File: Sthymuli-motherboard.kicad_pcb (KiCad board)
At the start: 2 copper layers, 176.5 x 154.2 mm, 270 parts, among them J1 USB_C_Receptacle_USB2.0_16P, J2 Conn_01x09, J3 Conn_01x03, J4 Conn_01x06, Q1 Q_NMOS_Depletion_GSD, Q10 NX7002AK, Q11 NX7002AK, Q12 NX7002AK, Q13 NX7002AK, Q14 NX7002AK, Q15 NX7002AK, Q2 Q_NMOS_Depletion_GSD, Q3 Q_NMOS_Depletion_GSD, Q4 Q_NMOS_Depletion_GSD, Q5 Q_NMOS_Depletion_GSD, Q6 Q_NMOS_Depletion_GSD, Q7 PMOS, Q8 NX7002AK, Q9 NX7002AK, SW1 SW_Push, SW10 SW_Push, SW2 SW_Push, SW3 SW_Push, SW4 SW_Push, SW5 SW_Push, SW6 SW_Push, SW7 SW_Push, SW8 SW_Push, SW9 SW_Push, U1 ESP32-S3-WROOM-1, U10 74HC4051, U11 MCP6L01x-xOT, U12 74HC4051, U13 LSM6DS3, U14 LSM6DS3, U15 ITR9909, U16 ITR9909, U17 ITR9909, U18 ITR9909, U19 ITR9909, U2 AP2112K-3.3, U20 ITR9909, U21 ITR9909, U22 ITR9909, U3 BQ76905RGRR, U4 AP62300WU, U5 BQ25713, U6 AP62300WU, U7 MCP23017_SO, U8 AP22913CN4, U9 IRM-H6xxT

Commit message: starting from scratch the routing. autorouter was not good
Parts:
- removed BT1, BT2, BT3: Battery_Cell, sthymuli:Battery_Holder_18650_robop
- removed C10, C11, C12, C13, C14, C15, C16, C17, C18, C19, C20, C21, C22, C23, C24, C25, C77, C8, C9: 100nF, Capacitor_SMD:C_0402_1005Metric
- removed D10, D11, D12, D13, D14, D15, D16, D17, D18, D19, D20, D21, D22, D23, D24, D25, D8, D9: WS2812B, LED_SMD:LED_WS2812B_PLCC4_5.0x5.0mm_P3.2mm
- removed D26, D27, D28: D_Schottky, Diode_SMD:D_SOD-123F
- removed F1, F2, F3: Fuse, Resistor_SMD:R_0805_2012Metric
- removed Q10, Q11, Q12, Q13, Q14, Q15: NX7002AK, Package_TO_SOT_SMD:SOT-23
- removed R52, R53, R54, R55, R56, R57: 3K3, Capacitor_SMD:C_0201_0603Metric
- removed R62, R63, R64, R65, R66, R67: 27R, Capacitor_SMD:C_0201_0603Metric
- removed SW10, SW5, SW6, SW7, SW8, SW9: SW_Push, sthymuli:XKB5858
- removed U13: LSM6DS3, Package_LGA:LGA-14_3x2.5mm_P0.5mm_LayoutBorder3x4y
- removed the U16 at (81.2, 89.6)
- removed U17, U18: ITR9909, sthymuli:ITR_9909_Horizontal
- removed U20, U21, U22: ITR9909, sthymuli:ITR_9909_Vertical
- added J11: Conn_02x08_Counter_Clockwise, Connector_PinSocket_2.54mm:PinSocket_2x08_P2.54mm_Vertical_SMD, B.Cu at (134.6, 75.5)
- added J12: Conn_02x08_Counter_Clockwise, Connector_PinSocket_2.54mm:PinSocket_2x08_P2.54mm_Vertical_SMD, B.Cu at (175.2, 75.5)
- added J8: Conn_02x08_Counter_Clockwise, Connector_PinSocket_2.54mm:PinSocket_2x08_P2.54mm_Vertical_SMD, B.Cu at (208.8, 103.4)
- J2: footprint Connector_PinHeader_2.54mm:PinHeader_1x09_P2.54mm_Vertical -> Connector_PinSocket_2.54mm:PinSocket_1x09_P2.54mm_Vertical_SMD_Pin1Left; moved to B.Cu
- J3: footprint Connector_PinHeader_2.54mm:PinHeader_1x03_P2.54mm_Vertical -> Connector_PinSocket_2.54mm:PinSocket_1x03_P2.54mm_Vertical_SMD_Pin1Left
- U16: renamed from U19; footprint sthymuli:ITR_9909_Vertical -> sthymuli:ITR_9909_Horizontal
- moved R20 260.2 mm to (170.7, 95.1), turned to -90 degrees
- moved R21 259.6 mm to (169.7, 95.2), turned to 90 degrees
- moved R34 257.4 mm to (167.7, 89.7), turned to -90 degrees
- moved R32 255.1 mm to (169.3, 103.0), turned to 180 degrees
- moved R43 254.0 mm to (171.0, 105.5), turned to 180 degrees
- moved R15 253.9 mm to (166.3, 96.1), turned to 90 degrees
- moved R17 253.6 mm to (164.6, 92.8), turned to 180 degrees
- moved C44 252.7 mm to (166.1, 103.5), turned to 180 degrees
- moved R36 252.5 mm to (171.4, 104.1), turned to 90 degrees
- moved R18 252.3 mm to (162.9, 92.8), turned to 180 degrees
- moved R37 251.8 mm to (170.4, 104.1), turned to 90 degrees
- moved R40 251.8 mm to (167.7, 94.8), turned to 180 degrees
- moved R25 251.4 mm to (167.3, 100.5), turned to 180 degrees
- moved C34 249.3 mm to (163.7, 95.0), turned to 180 degrees
- moved C43 249.1 mm to (168.9, 104.3), turned to 180 degrees
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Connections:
- net +BATT renamed WEST_BAT+
- net INT_WS2812_DIN renamed WS2812_DIN
- net Net-(BT3--) renamed EAST_BAT-
- net Net-(BT4--) renamed NORTH_BAT-
- J1 pad S1: GND -> (no net)
- Q8 pad 1: IR_TRA_0 -> NORTH_IR_TRA_HORI
- Q9 pad 1: IR_TRA_1 -> NORTH_IR_TRA_VERT
- R2 pad 1: Net-(BT1--) -> SOUTH_BAT+
- R3 pad 1: Net-(BT2--) -> EAST_BAT+
- R50 pad 2: IR_REC_0 -> NORTH_IR_REC_HORI
- R51 pad 2: IR_REC_1 -> NORTH_IR_REC_VERT
- SW3 pad 1: btn_NORTH_UP -> NORTH_btn_B
- SW4 pad 1: btn_NORTH_DOWN -> NORTH_btn_A
- U10 pad 1: IR_REC_4 -> SOUTH_IR_REC_VERT
- U10 pad 12: IR_REC_3 -> EAST_IR_REC_HORI
- U10 pad 13: IR_REC_0 -> NORTH_IR_REC_VERT
- U10 pad 14: IR_REC_1 -> NORTH_IR_REC_HORI
- U10 pad 15: IR_REC_2 -> EAST_IR_REC_VERT
- U10 pad 2: IR_REC_6 -> WEST_IR_REC_VERT
- U10 pad 4: IR_REC_7 -> WEST_IR_REC_HORI
- U10 pad 5: IR_REC_5 -> SOUTH_IR_REC_HORI
- U12 pad 1: IR_TRA_4 -> SOUTH_IR_TRA_VERT
- U12 pad 12: IR_TRA_3 -> EAST_IR_TRA_HORI
- U12 pad 13: IR_TRA_0 -> NORTH_IR_TRA_VERT
- U12 pad 14: IR_TRA_1 -> NORTH_IR_TRA_HORI
- U12 pad 15: IR_TRA_2 -> EAST_IR_TRA_VERT
- U12 pad 2: IR_TRA_6 -> WEST_IR_TRA_VERT
- U12 pad 4: IR_TRA_7 -> WEST_IR_TRA_HORI
- U12 pad 5: IR_TRA_5 -> SOUTH_IR_TRA_HORI
- U15 pad 4: IR_REC_0 -> NORTH_IR_REC_HORI
- U16 pad 1: Net-(Q12-D) -> Net-(Q9-D)
- U16 pad 2: Net-(R64-Pad1) -> Net-(R61-Pad1)
- U16 pad 4: IR_REC_4 -> NORTH_IR_REC_VERT
- U7 pad 1: btn_NORTH_UP -> NORTH_btn_A
- U7 pad 2: btn_NORTH_DOWN -> NORTH_btn_B
- U7 pad 3: btn_SOUTH_UP -> EAST_btn_A
- U7 pad 4: btn_SOUTH_DOWN -> EAST_btn_B
- U7 pad 5: btn_EAST_UP -> SOUTH_btn_A
- U7 pad 6: btn_EAST_DOWN -> SOUTH_btn_B
- U7 pad 7: btn_WEST_UP -> WEST_btn_A
- U7 pad 8: btn_WEST_DOWN -> WEST_btn_B
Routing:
- added copper zone on F.Cu, net GND
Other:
- board size 176.5 x 154.2 mm -> 153.6 x 66.2 mm
- copper layers 2 -> 4

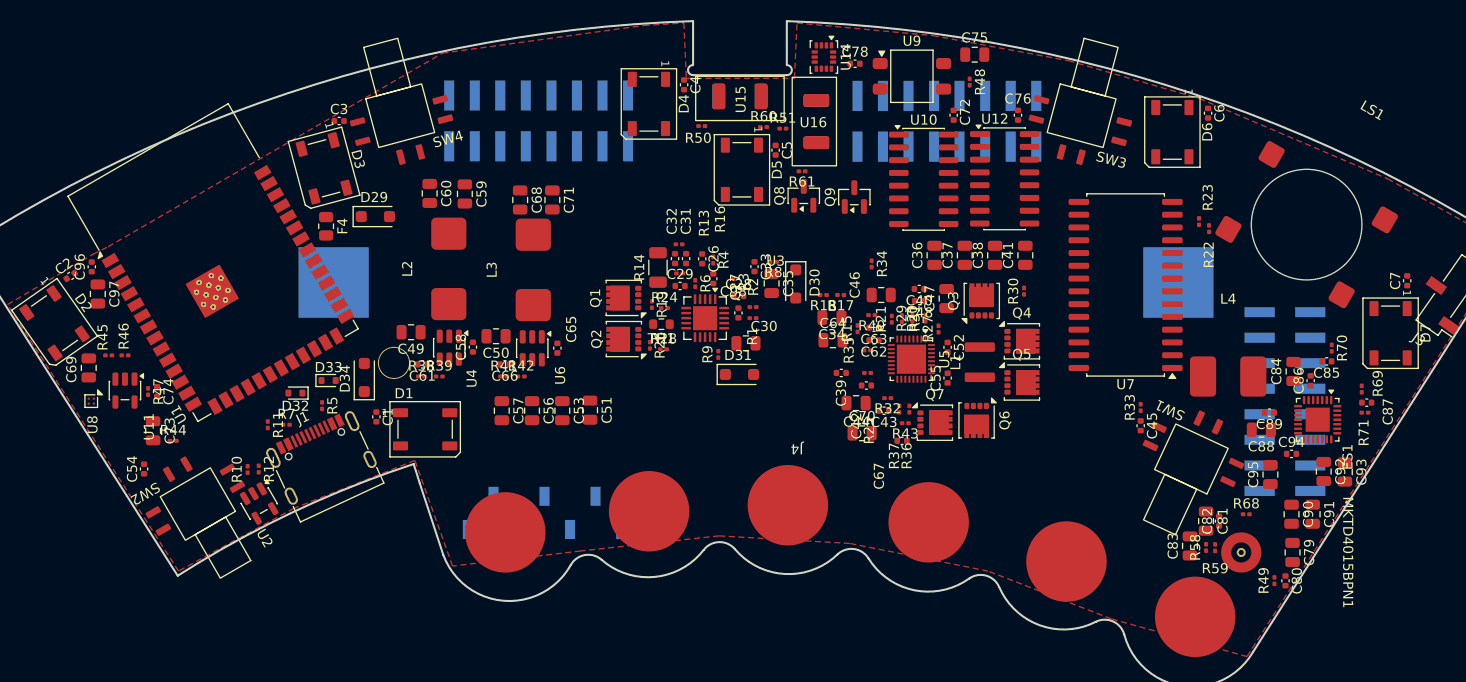
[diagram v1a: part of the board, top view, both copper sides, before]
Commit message: 280 left to route, power mostly done
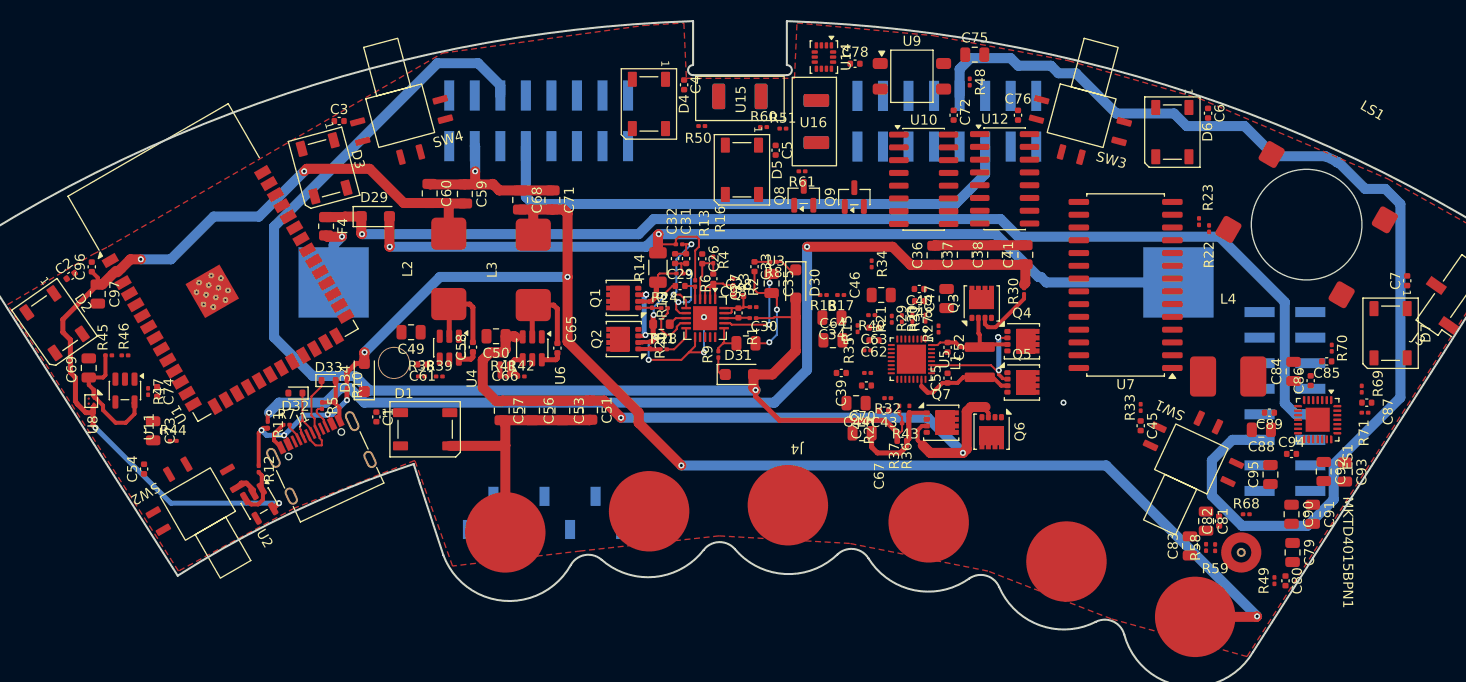
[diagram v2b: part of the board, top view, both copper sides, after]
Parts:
- moved R10 13.0 mm to (115.5, 101.8), turned to -90 degrees
- moved Q6 1.87 mm to (179.6, 106.4)
- moved Q7 0.62 mm to (174.6, 105.5)
- moved Q3 0.25 mm to (178.6, 93.6)
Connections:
- R11 pad 1: Net-(C36-Pad1) -> VBUS
- R11 pad 2: VBUS -> Net-(C36-Pad1)
- U2 pad 5: +3V3 -> Net-(U1-3V3)
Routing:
- net +5V: track 0.00 -> 135.4 mm, vias 0 -> 4
- net WEST_BAT+: track 0.00 -> 132.1 mm, vias 0 -> 1
- net EAST_BAT-: track 0.00 -> 114.2 mm, vias 0 -> 1
- net GND: track 0.00 -> 111.7 mm, vias 0 -> 14
- net EAST_BAT+: track 0.00 -> 108.5 mm
- net NORTH_BAT-: track 0.00 -> 95.5 mm, vias 0 -> 2
- net Net-(C36-Pad1): track 0.00 -> 94.5 mm, vias 0 -> 2
- net Net-(U1-3V3): track 0.00 -> 87.8 mm, vias 0 -> 4
- net Net-(Q6-D): track 0.00 -> 79.1 mm, vias 0 -> 2
- net SOUTH_BAT+: track 0.00 -> 55.0 mm
- net VBUS: track 0.00 -> 17.8 mm, vias 0 -> 3
- net Net-(Q7-D): track 0.00 -> 13.5 mm
- net +3V3: track 0.00 -> 12.9 mm
- net Net-(U3-BAT): track 0.00 -> 12.5 mm, vias 0 -> 2
- net Net-(U3-SRP): track 0.00 -> 11.0 mm, vias 0 -> 2
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
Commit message: 64 left to route
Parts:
- moved R34 3.80 mm to (171.2, 91.0)
- moved R20 0.45 mm to (170.2, 95.0)
- moved C52 0.37 mm to (175.5, 97.8)
- moved R29 0.28 mm to (172.0, 95.1)
- moved R21 0.27 mm to (169.5, 95.0)
- moved R31 0.22 mm to (173.2, 95.1)
- moved C55 0.19 mm to (175.2, 101.2)
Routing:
- net SDA: track 0.00 -> 259.7 mm, vias 0 -> 11
- net SCL: track 0.00 -> 213.9 mm, vias 0 -> 11
- net GND: track 111.7 -> 260.8 mm, vias 14 -> 15
- net RST: track 0.00 -> 126.7 mm, vias 0 -> 3
- net I2S_DOUT: track 0.00 -> 125.9 mm, vias 0 -> 4
- net I2S_MCLK: track 0.00 -> 125.3 mm, vias 0 -> 2
- net +5V: track 135.4 -> 254.7 mm, vias 4 -> 11
- net I2S_SCLK: track 0.00 -> 116.2 mm, vias 0 -> 2
- net I2S_LCLK: track 0.00 -> 115.2 mm, vias 0 -> 3
- net I2S_DSIN: track 0.00 -> 114.8 mm, vias 0 -> 3
- net IR_MODULATION: track 0.00 -> 114.1 mm, vias 0 -> 3
- net NORTH_btn_A: track 0.00 -> 111.8 mm, vias 0 -> 3
- net ACC_A_INT1: track 0.00 -> 106.2 mm, vias 0 -> 4
- net Net-(U10-A): track 0.00 -> 103.7 mm, vias 0 -> 3
- net GPIO_INTB: track 0.00 -> 103.1 mm, vias 0 -> 2
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- added copper zone on F.Cu, net GNDA

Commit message: done routing
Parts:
- U16: footprint sthymuli:ITR_9909_Horizontal -> sthymuli:ITR_9909_Vertical
- moved U16 0.69 mm to (162.8, 75.8), turned to 90 degrees
- moved R29 0.25 mm to (172.2, 95.1)
- moved C48 0.15 mm to (172.4, 93.2)
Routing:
- net GND: track 260.8 -> 603.2 mm, vias 15 -> 38
- net +3V3: track 115.0 -> 379.1 mm, vias 2 -> 17
- net +5V: track 254.7 -> 385.5 mm, vias 11 -> 17
- net PWR_ON: track 13.1 -> 63.7 mm, vias 2 -> 5
- net /MICBIAS: track 2.86 -> 50.7 mm, vias 0 -> 4
- net SCL: track 213.9 -> 234.4 mm
- net IR_S2: track 22.2 -> 38.4 mm, vias 3 -> 4
- net /D+: track 24.7 -> 36.9 mm, vias 2 -> 3
- net SOUTH_BAT+: track 55.0 -> 66.7 mm, vias 0 -> 2
- net GNDA: track 45.7 -> 56.0 mm
- net Net-(Q3-D): track 7.48 -> 17.4 mm, vias 0 -> 2
- net Net-(Q8-D): track 2.43 -> 11.7 mm, vias 1 -> 2
- net VBUS: track 25.8 -> 34.3 mm
- net EAST_BAT-: track 114.4 -> 122.8 mm, vias 1 -> 2
- net Net-(ES1-CCLK): track 0.00 -> 5.30 mm
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- added copper zone on B.Cu, net GND

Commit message: cleaning board
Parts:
- U1: footprint RF_Module:ESP32-S3-WROOM-1 -> sthymuli:ESP32-S3-WROOM-1
- moved J3 2.77 mm to (225.9, 90.1)
- moved C7 1.40 mm to (220.9, 90.0)
- moved C83 1.11 mm to (198.5, 118.5)
- moved J12 0.91 mm to (176.1, 75.5)
- moved C80 0.57 mm to (208.2, 121.2)
- moved R49 0.47 mm to (207.2, 121.2)
- moved SW2 0.32 mm to (100.7, 113.0)
- moved U2 0.30 mm to (106.8, 113.2)
- moved C82 0.28 mm to (202.5, 115.3)
- moved C4 0.10 mm to (149.0, 72.0)
- moved R12 0.10 mm to (106.7, 110.0)
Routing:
- net GND: track 603.2 -> 695.8 mm, vias 38 -> 37
- net /MICBIAS: track 50.7 -> 21.9 mm, vias 4 -> 2
- net GNDA: track 56.0 -> 72.1 mm
- net VBUS: track 34.3 -> 23.8 mm
- net I2S_DSIN: track 119.4 -> 115.0 mm
- net SCL: track 234.4 -> 230.2 mm
- net Net-(Q6-D): track 98.5 -> 95.0 mm
- net NORTH_BAT-: track 99.7 -> 96.3 mm
- net SOUTH_IR_REC_HORI: track 6.78 -> 9.98 mm
- net WEST_BAT+: track 134.1 -> 131.1 mm
- net EAST_IR_REC_VERT: track 55.5 -> 53.2 mm
- net SOUTH_btn_A: track 43.0 -> 40.8 mm
- net EXT_GPIO_2: track 60.8 -> 58.6 mm
- net NORTH_IR_TRA_HORI: track 34.3 -> 36.4 mm
- net EAST_BAT+: track 150.6 -> 148.6 mm
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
